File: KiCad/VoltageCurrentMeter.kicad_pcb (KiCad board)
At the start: 2 copper layers, 64.6 x 41.8 mm, 69 parts, among them J1 CHAN-1, J10 Power Jumper, J11 Daughter Board 1, J12 Daughter Board 2, J2 CHAN-2, J3 CHAN-3, J4 CHAN-4, J5 CHAN-5, J6 CHAN-6, J7 CHAN-7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

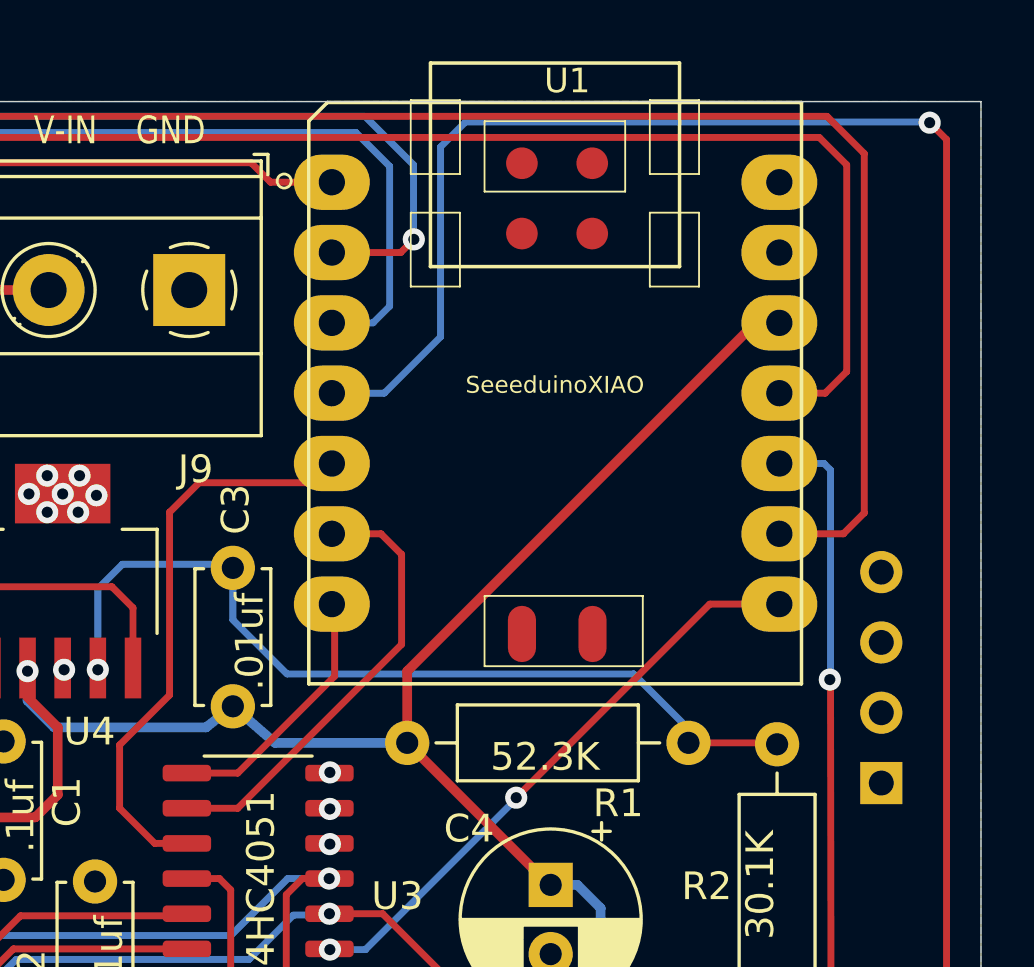
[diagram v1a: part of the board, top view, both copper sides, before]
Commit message: Fixed an issue where the pins on the Seeeduino XIAO were a little too far apart.
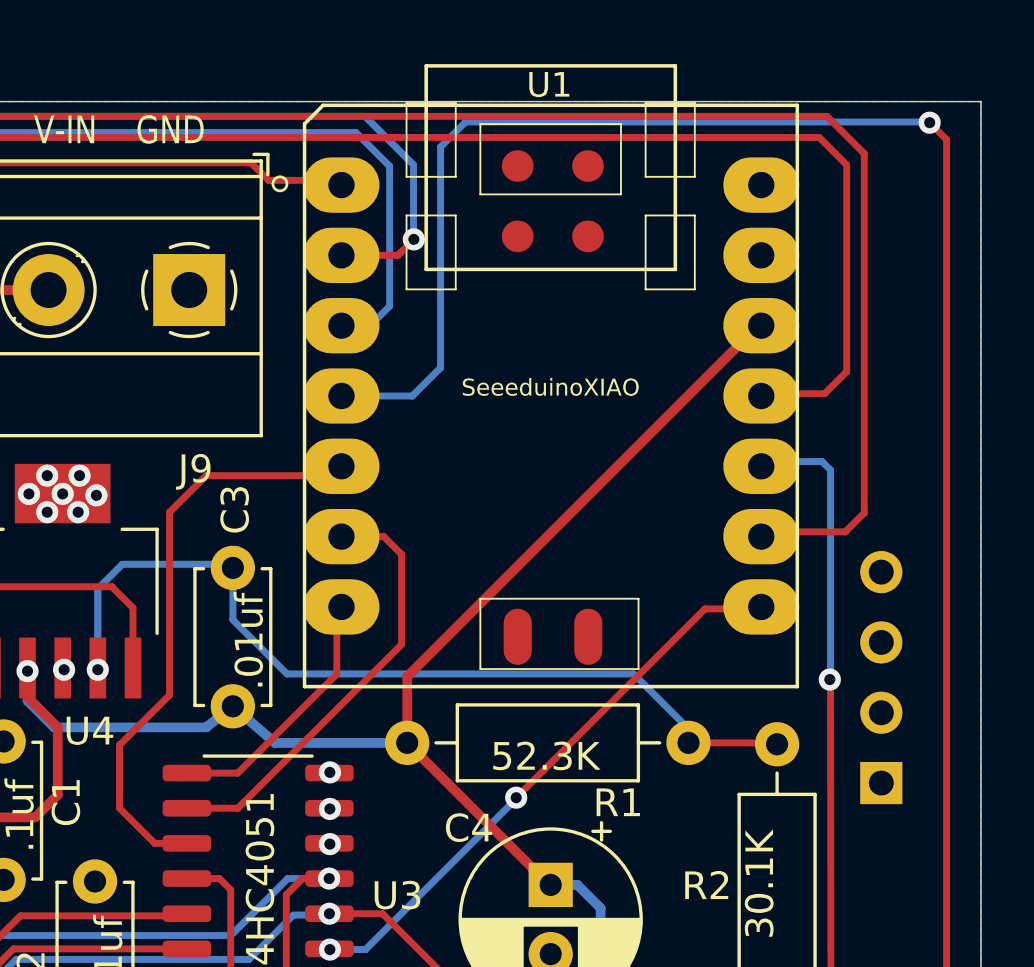
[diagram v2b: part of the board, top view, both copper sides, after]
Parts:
- moved U1 0.18 mm to (90.4, 103.1)
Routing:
- net Net-(J12-Pad4): track 103.9 -> 104.6 mm
- net Net-(U1-Pad3): track 134.8 -> 135.5 mm
- net Net-(U1-Pad8): track 95.3 -> 96.0 mm
- net Net-(U1-Pad10): track 90.3 -> 91.0 mm
- net Net-(U1-Pad7): track 21.4 -> 20.7 mm
